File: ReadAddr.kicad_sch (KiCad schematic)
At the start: 8 parts, among them U501 74HC163, U502 74HC163, U503 74HC163, U504 74HC163

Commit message: start working on VRAM/read logic
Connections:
- net VCC: now also U502.16 (VCC)
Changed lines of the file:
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@@
 	(wire
 		(pts
-			(xy 110.49 96.52) (xy 110.49 99.06)
+			(xy 110.49 99.06) (xy 110.49 101.6)
 		)
 		(stroke
@@
 	(symbol
 		(lib_id "power:VCC")
-		(at 110.49 96.52 0)
+		(at 110.49 99.06 0)
 		(unit 1)
 		(exclude_from_sim no)
@@
 		(fields_autoplaced yes)
 		(property "Reference" "#PWR048"
-			(at 110.49 100.33 0)
+			(at 110.49 102.87 0)
 			(effects
 				(font
@@
 		)
 		(property "Value" "VCC"
-			(at 110.49 91.44 0)
+			(at 110.49 93.98 0)
 			(effects
 				(font
@@
 		)
 		(property "Footprint" ""
-			(at 110.49 96.52 0)
+			(at 110.49 99.06 0)
 			(effects
 				(font
@@
 		)
 		(property "Datasheet" ""
-			(at 110.49 96.52 0)
+			(at 110.49 99.06 0)
 			(effects
 				(font
@@
 		)
 		(property "Description" "Power symbol creates a global label with name \"VCC\""
-			(at 110.49 96.52 0)
-			(effects
-				(font
+			(at 110.49 99.06 0)
+			(effects
+				(font

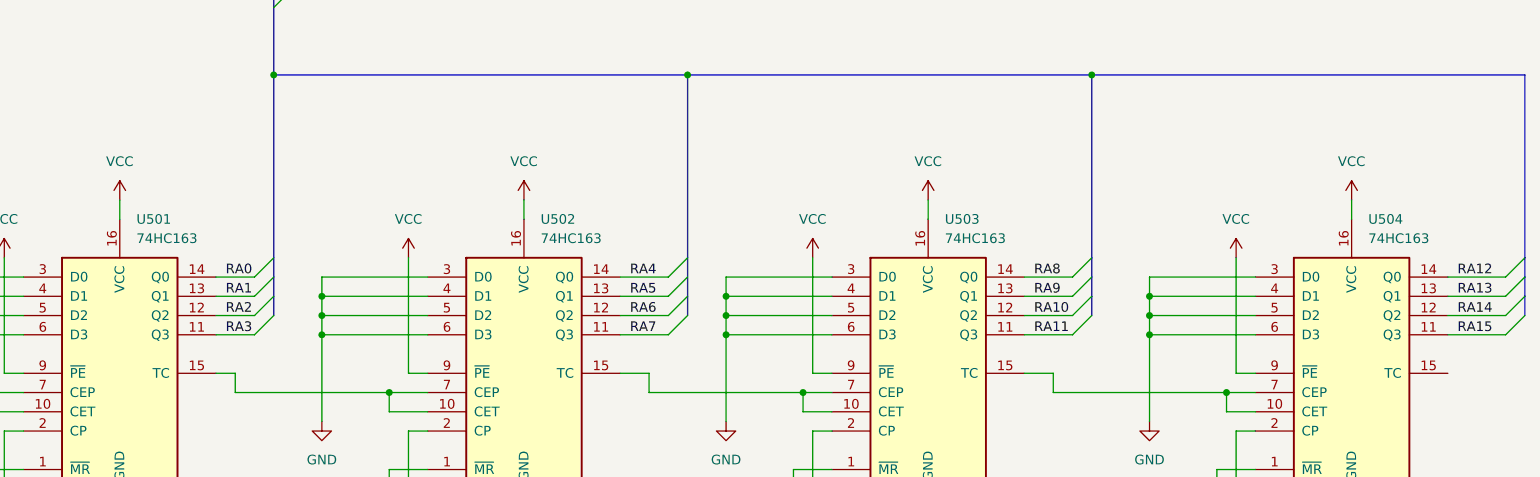
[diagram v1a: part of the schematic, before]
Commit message: chips driven by GAL or memory need to be 74HCT
I forgot that GALs only guarantee 2.4V as the minimum
output high voltage. Bleh.
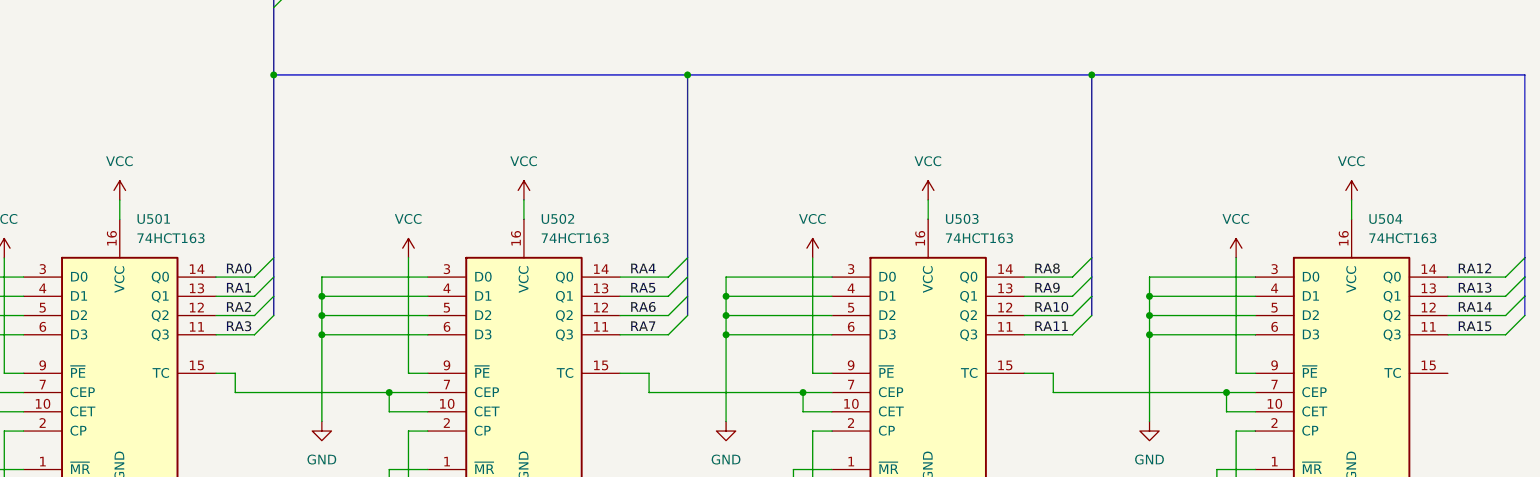
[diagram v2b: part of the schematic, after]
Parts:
- U501, U502, U503, U504: value 74HC163 -> 74HCT163
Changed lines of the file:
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@@
 			)
 		)
-		(property "Value" "74HC163"
+		(property "Value" "74HCT163"
 			(at 112.6841 104.14 0)
 			(effects
@@
 			)
 		)
-		(property "Value" "74HC163"
+		(property "Value" "74HCT163"
 			(at 59.3441 104.14 0)
 			(effects
@@
 			)
 		)
-		(property "Value" "74HC163"
+		(property "Value" "74HCT163"
 			(at 221.9041 104.14 0)
 			(effects
@@
 			)
 		)
-		(property "Value" "74HC163"
+		(property "Value" "74HCT163"
 			(at 166.0241 104.14 0)
 			(effects
